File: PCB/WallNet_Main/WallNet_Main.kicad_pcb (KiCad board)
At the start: 4 copper layers, 120 x 70.2 mm, 86 parts, among them J1 Conn_01x05_Pin, J101 USB_C_Receptacle_PowerOnly_6P, J102 01x04 Molex, J2 Conn_01x05_Pin, J201 01x04 Molex, J203 02x12 Connector, Q201 BSS138, SW1 SW, U1 BT832, U101 BQ25895RTWT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

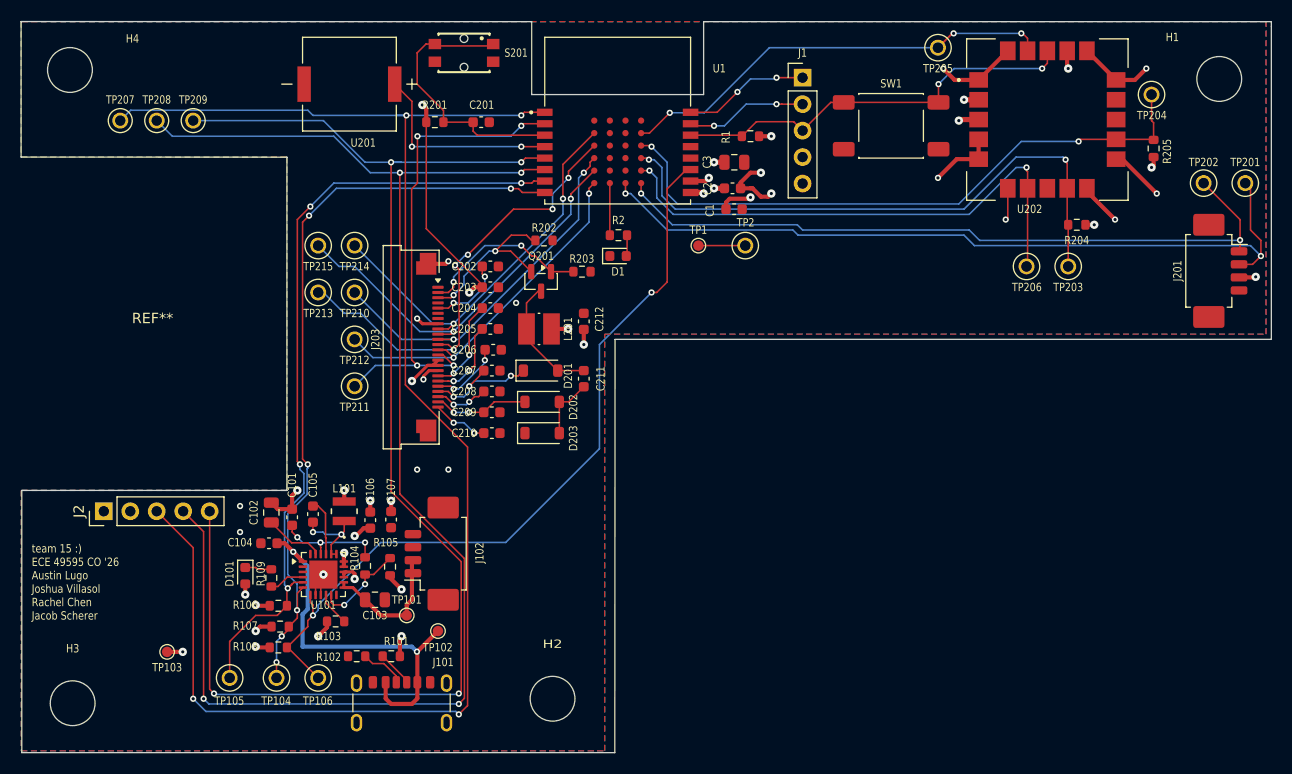
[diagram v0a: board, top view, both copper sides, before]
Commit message: Redid PCB still need to DRC the design
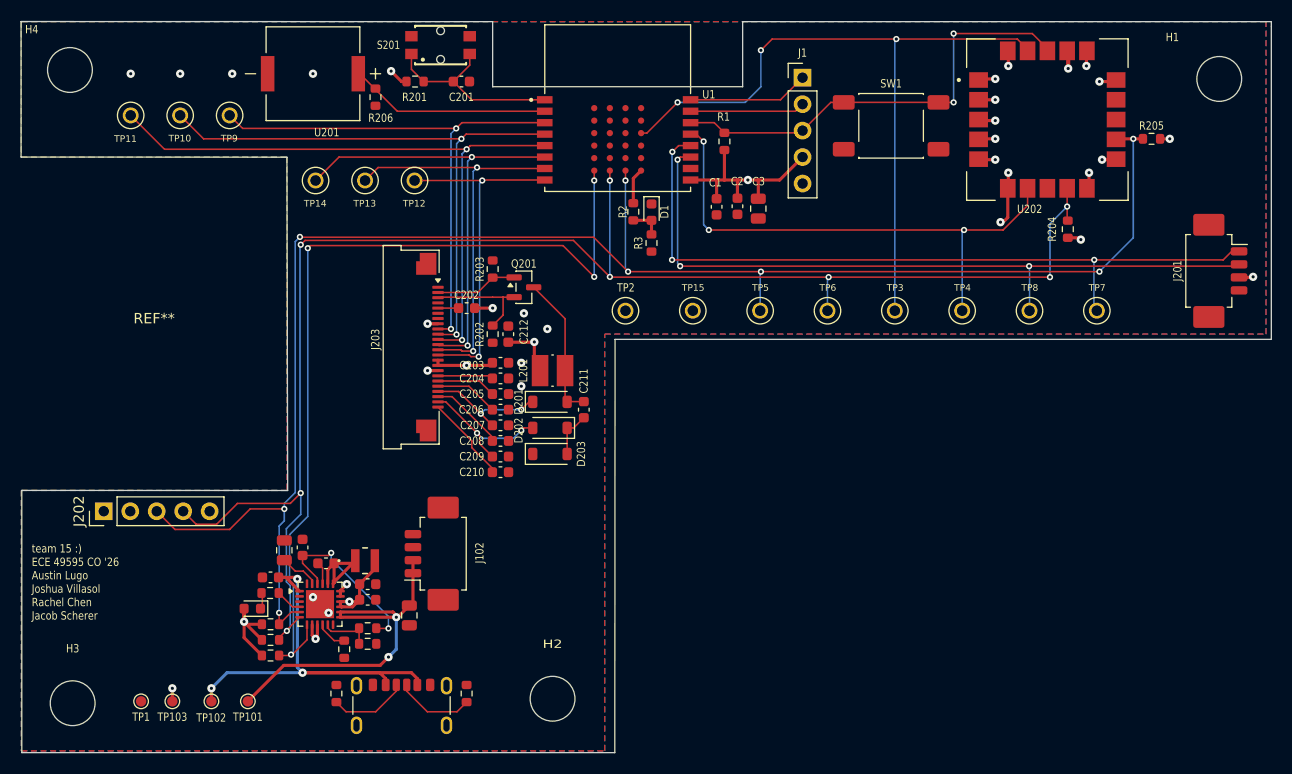
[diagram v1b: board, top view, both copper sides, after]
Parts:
- removed TP104: BQ_SDA, 5001:KEYSTONE_5001
- removed TP105: BQ_SCL, 5001:KEYSTONE_5001
- removed TP106: BQ_INT, 5001:KEYSTONE_5001
- removed TP201: TS_TX, 5001:KEYSTONE_5001
- removed TP202: TS_RX, 5001:KEYSTONE_5001
- removed TP203: GPS_SDA, 5001:KEYSTONE_5001
- removed TP204: GPS_SCL, 5001:KEYSTONE_5001
- removed TP205: GPS_INT, 5001:KEYSTONE_5001
- removed TP206: GPS_TP, 5001:KEYSTONE_5001
- removed TP207: RFID_SCL, 5001:KEYSTONE_5001
- removed TP208: RFID_SDA, 5001:KEYSTONE_5001
- removed TP209: RFID_GPO, 5001:KEYSTONE_5001
- removed TP210: EP_DC, 5001:KEYSTONE_5001
- removed TP211: EP_SDA, 5001:KEYSTONE_5001
- removed TP212: EP_SCL, 5001:KEYSTONE_5001
- removed TP213: EP_CSB, 5001:KEYSTONE_5001
- removed TP214: EP_BUSY, 5001:KEYSTONE_5001
- removed TP215: EP_RESET, 5001:KEYSTONE_5001
- added R206: 10k, Resistor_SMD:R_0603_1608Metric, F.Cu at (46.0, 18.8)
- added R3: 10k, Resistor_SMD:R_0603_1608Metric, F.Cu at (72.5, 32.8)
- added TP10: EP_RESET, 5001:KEYSTONE_5001, F.Cu at (27.2, 20.5)
- added TP11: EP_DC, 5001:KEYSTONE_5001, F.Cu at (22.5, 20.5)
- added TP12: EP_DIN, 5001:KEYSTONE_5001, F.Cu at (49.8, 26.8)
- added TP13: EP_SCL, 5001:KEYSTONE_5001, F.Cu at (45.0, 26.8)
- added TP14: EP_CSB, 5001:KEYSTONE_5001, F.Cu at (40.2, 26.8)
- added TP15: GND, 5001:KEYSTONE_5001, F.Cu at (76.5, 39.2)
- added TP3: GPS_INT, 5001:KEYSTONE_5001, F.Cu at (95.9, 39.2)
- added TP4: GPS_TP, 5001:KEYSTONE_5001, F.Cu at (102.3, 39.2)
- added TP5: SCL, 5001:KEYSTONE_5001, F.Cu at (82.9, 39.2)
- added TP6: SDA, 5001:KEYSTONE_5001, F.Cu at (89.4, 39.2)
- added TP7: RX, 5001:KEYSTONE_5001, F.Cu at (115.2, 39.2)
- added TP8: TX, 5001:KEYSTONE_5001, F.Cu at (108.8, 39.2)
- added TP9: EP_BUSY, 5001:KEYSTONE_5001, F.Cu at (32.0, 20.5)
- moved TP1 69.1 mm to (23.5, 76.8)
- moved TP102 22.8 mm to (30.2, 76.8)
- moved TP101 17.3 mm to (33.8, 76.8)
- moved TP2 13.1 mm to (70.0, 39.2)
- moved R202 10.3 mm to (57.2, 41.5), turned to 90 degrees
- moved R203 8.58 mm to (57.2, 35.2), turned to -90 degrees
- moved R101 8.07 mm to (54.8, 76.0), turned to 90 degrees
- moved R105 7.71 mm to (45.2, 71.2), turned to 0 degrees
- moved C106 7.65 mm to (45.2, 67.0), turned to 0 degrees
- moved C212 7.35 mm to (58.8, 41.5)
- moved C203 7.32 mm to (58.0, 44.2)
- moved C204 6.82 mm to (58.0, 45.8)
- moved C107 6.60 mm to (45.2, 65.5), turned to 0 degrees
- moved C205 6.33 mm to (58.0, 47.2)
- moved R104 5.99 mm to (45.2, 69.7), turned to 180 degrees
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- renumbered J2 to J202
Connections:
- net /Battery/BAT renamed /Power/BAT
- net /Battery/BTST renamed /Power/BTST
- net /Battery/ILIM renamed /Power/ILIM
- net /Battery/PMID renamed /Power/PMID
- net /Battery/REGN renamed /Power/REGN
- net /Battery/STAT renamed /Power/STAT
- net /Battery/SW renamed /Power/SW
- net /Battery/TS renamed /Power/TS
- net /Battery/VBUS_BQ renamed /Power/VBUS_BQ
- C201 pad 1: /P00 -> /P26
- C211 pad 2: Net-(D202-A) -> Net-(D202-K)
- D202 pad 1: /Sensors/VGL -> Net-(D202-K)
- D202 pad 2: Net-(D202-A) -> /Sensors/VGL
- D203 pad 2: Net-(D202-A) -> Net-(D202-K)
- J201 pad 1: /P11 -> /P18
- J201 pad 2: /P12 -> /P13
- J202 pad 3: /P26 -> /P12
- J202 pad 4: /P03 -> /P08
- J202 pad 5: /P02 -> /Sensors/RFID_GPO
- J203 pad 10: /P05 -> /P01
- J203 pad 11: /P04 -> /P02
- J203 pad 12: /P29 -> /P03
- J203 pad 13: /P07 -> /P09
- J203 pad 14: /P27 -> /P10
- J203 pad 9: /P28 -> /P00
- R106 pad 2: /P09 -> /P12
- R107 pad 2: /P10 -> /P08
- R108 pad 2: /P13 -> /P07
- R2 pad 1: /P08 -> /P11
- R201 pad 2: /P00 -> /P26
- R204 pad 2: /P16 -> /P08
- R205 pad 2: /P19 -> /P12
- S201 pad 1: /P00 -> /P26
- S201 pad 3: /P00 -> /P26
- U101 pad 5: /P09 -> /P12
- U101 pad 6: /P10 -> /P08
- U101 pad 7: /P13 -> /P07
- U201 pad P: /P01 -> /P27
- U202 pad 12: /P19 -> /P12
- U202 pad 19: /P23 -> /P19
- U202 pad 7: /P14 -> /P20
- U202 pad 9: /P16 -> /P08
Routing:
- net /P08: track 5.00 -> 152.0 mm, vias 0 -> 8
- net /P26: track 148.4 -> 18.8 mm, vias 4 -> 0
- net /P03: track 136.8 -> 44.1 mm, vias 4 -> 2
- net /P12: track 74.5 -> 163.3 mm, vias 2 -> 8
- net /P18: track 0.00 -> 71.8 mm, vias 0 -> 3
- net /P02: track 131.7 -> 62.1 mm, vias 4 -> 2
- net /P11: track 68.9 -> 3.44 mm, vias 2 -> 0
- net /P16: track 56.4 -> 0.00 mm, vias 2 -> 0
- net /P20: track 0.00 -> 51.3 mm, vias 0 -> 3
- net /P14: track 50.8 -> 0.00 mm, vias 2 -> 0
- net /P07: track 34.4 -> 83.9 mm, vias 2 -> 4
- net /P29: track 45.1 -> 0.00 mm, vias 5 -> 0
- net /P23: track 44.6 -> 0.00 mm, vias 3 -> 0
- net GND: track 70.6 -> 27.4 mm, vias 24 -> 25
- net /P10: track 73.1 -> 33.5 mm, vias 6 -> 2
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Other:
- outline, holes or cut-outs redrawn

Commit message: Finish layout
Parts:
- moved C201 1.05 mm to (53.2, 17.2)
- moved R201 1.05 mm to (48.8, 17.2)
- moved S201 1.05 mm to (51.2, 13.8)
- moved L101 0.19 mm to (45.2, 63.2)
- turned R202 to -90 degrees
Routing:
- net /P26: track 18.8 -> 21.9 mm
- net /Sensors/RESE: track 10.5 -> 13.6 mm, vias 0 -> 2
- net /P12: track 163.3 -> 164.5 mm
- net /P20: track 51.3 -> 52.4 mm
- net /P08: track 152.0 -> 153.0 mm
- net /P07: track 83.9 -> 84.7 mm

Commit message: Fixed minor Issues
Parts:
- C105: value 4.7uF -> 47nF
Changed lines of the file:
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@@
 			)
 		)
-		(property "Value" "4.7uF"
+		(property "Value" "47nF"
 			(at 0 -1 0)
 			(layer "F.Fab")

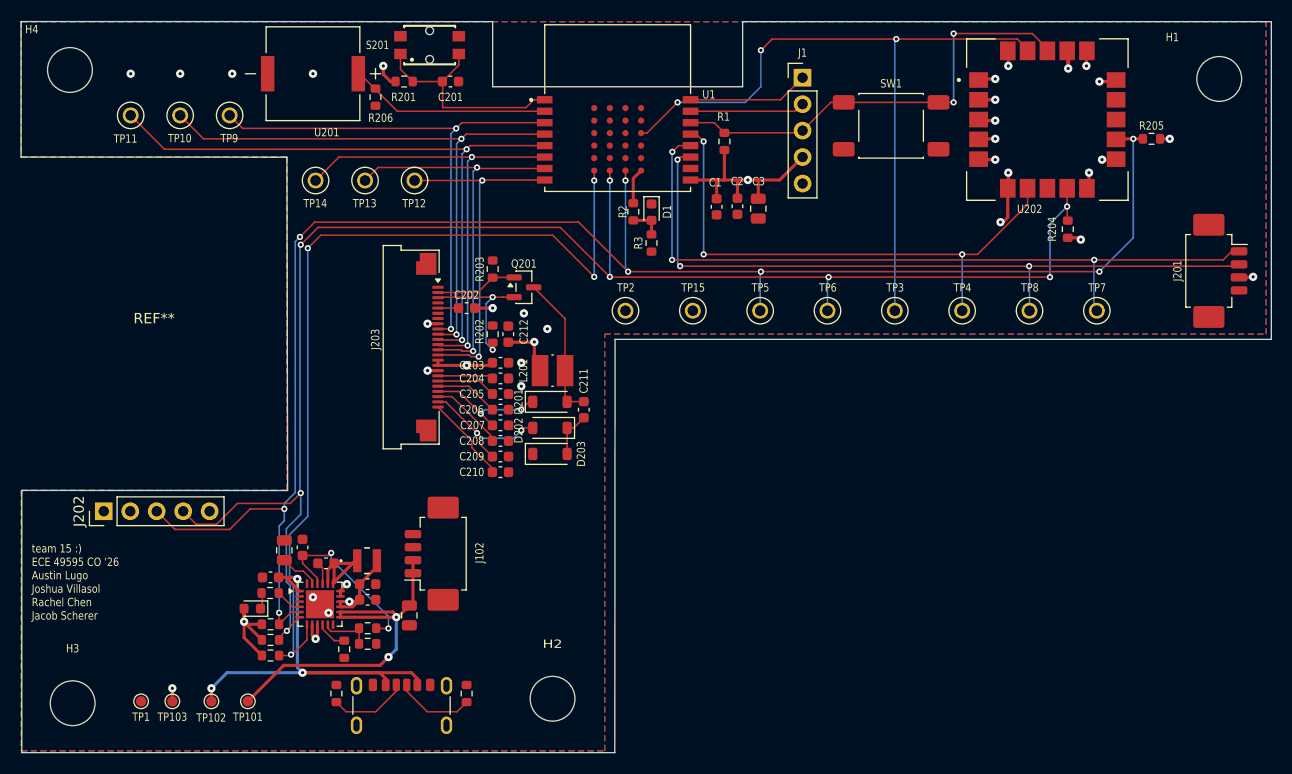
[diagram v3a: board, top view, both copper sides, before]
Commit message: Fixed position of mounting holes
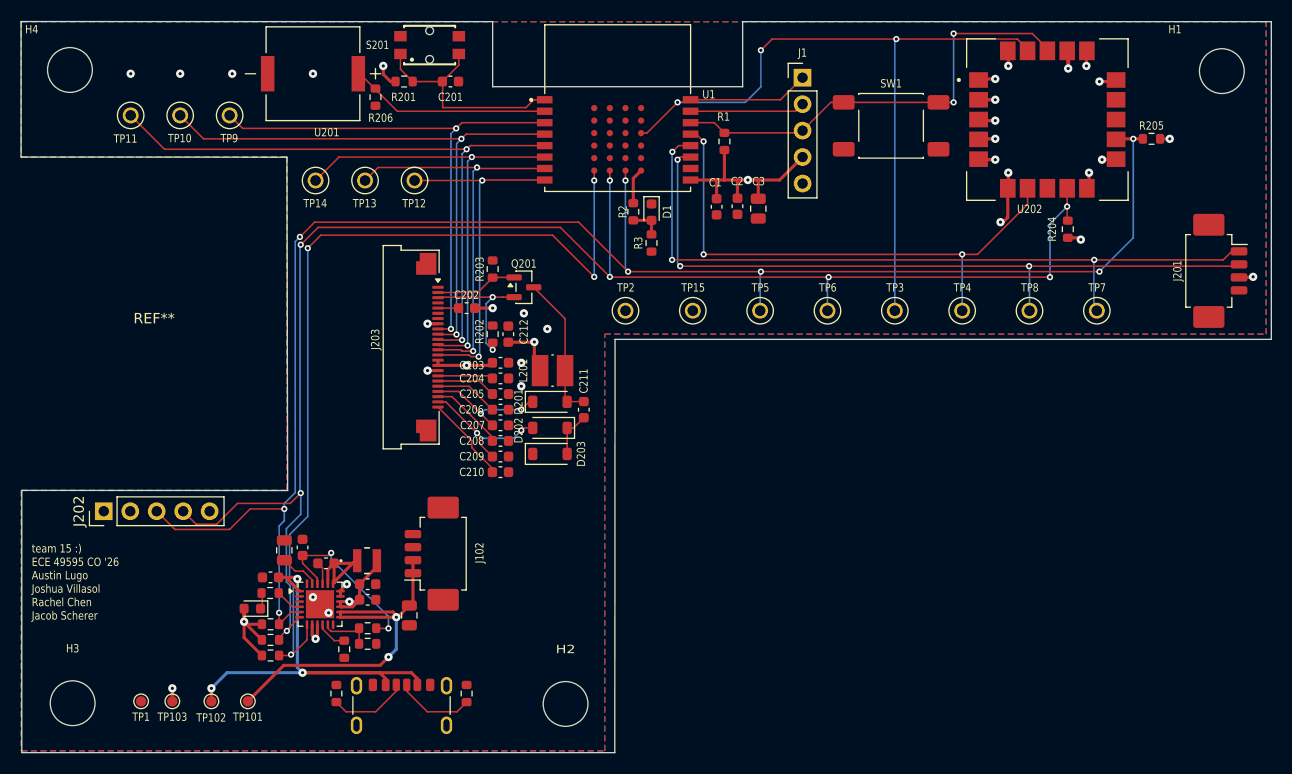
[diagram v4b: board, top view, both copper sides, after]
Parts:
- moved H2 1.35 mm to (64.2, 77.0)
- moved H1 0.79 mm to (127.2, 16.2)
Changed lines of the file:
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@@
 	(footprint "MountingHole:MountingHole_4.3mm_M4"
 		(layer "F.Cu")
-		(at 127 17)
+		(at 127.25 16.25)
 		(descr "Mounting Hole 4.3mm, M4, no annular, generated by kicad-footprint-generator mountinghole.py")
 		(tags "mountinghole M4")
@@
 	(footprint "MountingHole:MountingHole_4.3mm_M4"
 		(layer "F.Cu")
-		(at 63 76.5)
+		(at 64.25 77)
 		(descr "Mounting Hole 4.3mm, M4, no annular, generated by kicad-footprint-generator mountinghole.py")
 		(tags "mountinghole M4")

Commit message: Implemented most changes
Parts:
- added D2: LED, Diode_SMD:D_0603_1608Metric, F.Cu at (76.5, 29.8)
- added R4: 240, Resistor_SMD:R_0603_1608Metric, F.Cu at (75.0, 29.8)
- added R5: 10k, Resistor_SMD:R_0603_1608Metric, F.Cu at (77.2, 32.1)
- added TP16: Pad, TestPoint:TestPoint_Pad_1.0x1.0mm, F.Cu at (51.0, 72.0)
- added TP17: Pad, TestPoint:TestPoint_Pad_1.0x1.0mm, F.Cu at (53.8, 72.0)
- added TP18: Pad, TestPoint:TestPoint_Pad_1.0x1.0mm, F.Cu at (56.7, 72.0)
- added TP19: Pad, TestPoint:TestPoint_Pad_1.0x1.0mm, F.Cu at (59.5, 72.0)
- moved SW1 6.33 mm to (89.2, 20.5), turned to 90 degrees
- moved J1 3.47 mm to (83.8, 15.7)
- moved C1 0.50 mm to (79.2, 29.2)
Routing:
- net /P28: track 0.00 -> 57.6 mm, vias 0 -> 2
- net /P29: track 0.00 -> 55.3 mm, vias 0 -> 2
- net /P04: track 0.00 -> 52.9 mm, vias 0 -> 2
- net /P05: track 0.00 -> 50.5 mm, vias 0 -> 2
- net /P14: track 0.00 -> 5.77 mm
- net RESET: track 43.3 -> 47.4 mm
- net Net-(D2-A): track 0.00 -> 3.03 mm
- net /SWDCLK: track 11.0 -> 8.28 mm
- net /SWDIO: track 11.6 -> 9.11 mm
- net /P19: track 69.6 -> 71.0 mm
- net VDD_nrf: track 63.3 -> 62.1 mm
- net /Power/VBUS_BQ: track 44.9 -> 45.9 mm
- net GND: vias 25 -> 39

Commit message: Acute angles destroyed
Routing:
- net /Power/VBUS_BQ: track 45.9 -> 44.6 mm
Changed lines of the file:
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@@
 	(segment
 		(start 36.7 64.85)
-		(end 37.3875 64.85)
+		(end 38.35 64.85)
 		(width 0.3)
 		(layer "F.Cu")
@@
 	)
 	(segment
-		(start 37.3875 64.85)
-		(end 38.7125 66.175)
+		(start 38.5 65)
+		(end 38.5 65.9625)
 		(width 0.3)
 		(layer "F.Cu")
@@
 	)
 	(segment
-		(start 36.7 64.85)
-		(end 38.35 64.85)
+		(start 38.5 65.9625)
+		(end 38.7125 66.175)
 		(width 0.3)
 		(layer "F.Cu")
